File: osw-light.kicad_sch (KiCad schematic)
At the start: 53 parts, among them J1 Conn_01x02, J2 USB_C_Receptacle_USB2.0, Q1 2N7002, SW1 SW_Push, SW2 SW_Push, SW4 SW_Push, SW5 SW_Push, U1 DS3231MZ, U10 XC6209, U11 MCP73831T-2ACI_OT, U13 XC6209, U2 BMA400, U4 GC9A01_IPS_display, U6 CH340E, U7 ttgo-32-micro, U9 TPS2115A

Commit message: fixed some footprints and other stuff
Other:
- moved on the sheet: J2, R2, R3
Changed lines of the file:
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@@
   (junction (at 33.02 156.21) (diameter 0) (color 0 0 0 0)
   )
-  (junction (at 356.87 63.5) (diameter 0) (color 0 0 0 0)
+  (junction (at 340.995 72.39) (diameter 0) (color 0 0 0 0)
   )
   (junction (at 159.385 172.72) (diameter 0) (color 0 0 0 0)
@@
   (no_connect (at 217.17 86.36))
   (no_connect (at 29.21 86.36))
-  (no_connect (at 342.265 83.82))
-  (no_connect (at 342.265 86.36))
+  (no_connect (at 326.39 92.71))
+  (no_connect (at 326.39 95.25))
   (polyline (pts (xy 208.28 114.935) (xy 281.94 114.935))
     (stroke (width 0) (type default) (color 0 0 0 0))
   )
-  (wire (pts (xy 342.265 60.96) (xy 349.885 60.96))
+  (wire (pts (xy 326.39 69.85) (xy 334.01 69.85))
     (stroke (width 0) (type default) (color 0 0 0 0))
   )
@@
     (stroke (width 0) (type default) (color 0 0 0 0))
   )
-  (wire (pts (xy 354.965 60.96) (xy 356.87 60.96))
+  (wire (pts (xy 339.09 69.85) (xy 340.995 69.85))
     (stroke (width 0) (type default) (color 0 0 0 0))
   )
@@
     (stroke (width 0) (type default) (color 0 0 0 0))
   )
-  (wire (pts (xy 356.87 63.5) (xy 356.87 65.405))
+  (wire (pts (xy 340.995 72.39) (xy 340.995 74.295))
     (stroke (width 0) (type default) (color 0 0 0 0))
   )
@@
     (stroke (width 0) (type default) (color 0 0 0 0))
   )
-  (wire (pts (xy 342.265 73.66) (xy 342.265 76.2))
+  (wire (pts (xy 326.39 82.55) (xy 326.39 85.09))
     (stroke (width 0) (type default) (color 0 0 0 0))
   )
@@
     (stroke (width 0) (type default) (color 0 0 0 0))
   )
-  (wire (pts (xy 342.265 68.58) (xy 342.265 71.12))
+  (wire (pts (xy 326.39 77.47) (xy 326.39 80.01))
     (stroke (width 0) (type default) (color 0 0 0 0))
   )
@@
     (stroke (width 0) (type default) (color 0 0 0 0))
   )
-  (wire (pts (xy 356.87 63.5) (xy 349.885 63.5))
+  (wire (pts (xy 340.995 72.39) (xy 334.01 72.39))
     (stroke (width 0) (type default) (color 0 0 0 0))
   )
@@
     (stroke (width 0) (type default) (color 0 0 0 0))
   )
-  (wire (pts (xy 342.265 55.88) (xy 347.345 55.88))
+  (wire (pts (xy 326.39 64.77) (xy 331.47 64.77))
     (stroke (width 0) (type default) (color 0 0 0 0))
   )
@@
     (stroke (width 0) (type default) (color 0 0 0 0))
   )
-  (wire (pts (xy 327.025 93.98) (xy 327.025 95.885))
+  (wire (pts (xy 311.15 102.87) (xy 311.15 104.775))
     (stroke (width 0) (type default) (color 0 0 0 0))
   )
@@
     (stroke (width 0) (type default) (color 0 0 0 0))
   )
-  (wire (pts (xy 342.265 63.5) (xy 344.805 63.5))
+  (wire (pts (xy 326.39 72.39) (xy 328.93 72.39))
     (stroke (width 0) (type default) (color 0 0 0 0))
   )
@@
     (stroke (width 0) (type default) (color 0 0 0 0))
   )
-  (wire (pts (xy 356.87 60.96) (xy 356.87 63.5))
+  (wire (pts (xy 340.995 69.85) (xy 340.995 72.39))
     (stroke (width 0) (type default) (color 0 0 0 0))
   )
@@
     (effects (font (size 1.27 1.27)) (justify left bottom))
   )
-  (label "D_N" (at 342.265 71.12 0)
-    (effects (font (size 1.27 1.27)) (justify left bottom))
-  )
-  (label "VBUS" (at 347.345 55.88 180)
+  (label "D_N" (at 326.39 80.01 0)
+    (effects (font (size 1.27 1.27)) (justify left bottom))
+  )
+  (label "VBUS" (at 331.47 64.77 180)
     (effects (font (size 1.27 1.27)) (justify right bottom))
   )
@@
     (effects (font (size 1.27 1.27)) (justify left bottom))
   )
-  (label "CC2" (at 342.392 63.5 0)
+  (label "CC2" (at 326.517 72.39 0)
     (effects (font (size 1.27 1.27)) (justify left bottom))
   )
@@
     (effects (font (size 1.27 1.27)) (justify left bottom))
   )
-  (label "D_P" (at 342.265 76.2 0)
+  (label "D_P" (at 326.39 85.09 0)
     (effects (font (size 1.27 1.27)) (justify left bottom))
   )
@@
     (effects (font (size 1.27 1.27)) (justify right bottom))
   )
-  (label "CC1" (at 342.392 60.96 0)
+  (label "CC1" (at 326.517 69.85 0)
     (effects (font (size 1.27 1.27)) (justify left bottom))
   )
@@
     (pin "1")
   )
-  (symbol (lib_id "Connector:USB_C_Receptacle_USB2.0") (at 327.025 71.12 0) (unit 1)
+  (symbol (lib_id "Connector:USB_C_Receptacle_USB2.0") (at 311.15 80.01 0) (unit 1)
     (in_bom yes) (on_board yes) (fields_autoplaced)
-    (property "Reference" "J2" (id 0) (at 327.025 48.26 0))
-    (property "Value" "USB_C_Receptacle_USB2.0" (id 1) (at 327.025 50.8 0))
-    (property "Footprint" "sat1l:GCT_USB4105-GF-A" (id 2) (at 330.835 71.12 0)
-      (effects (font (size 1.27 1.27)) hide)
-    )
-    (property "Datasheet" "https://www.usb.org/sites/default/files/documents/usb_type-c.zip" (id 3) (at 330.835 71.12 0)
+    (property "Reference" "J2" (id 0) (at 311.15 57.15 0))
+    (property "Value" "USB_C_Receptacle_USB2.0" (id 1) (at 311.15 59.69 0))
+    (property "Footprint" "sat1l:GCT_USB4105-GF-A" (id 2) (at 314.96 80.01 0)
+      (effects (font (size 1.27 1.27)) hide)
+    )
+    (property "Datasheet" "https://www.usb.org/sites/default/files/documents/usb_type-c.zip" (id 3) (at 314.96 80.01 0)
       (effects (font (size 1.27 1.27)) hide)
     )
@@
     (pin "S1")
   )
-  (symbol (lib_id "Device:R_Small") (at 347.345 63.5 90) (unit 1)
+  (symbol (lib_id "Device:R_Small") (at 331.47 72.39 90) (unit 1)
     (in_bom yes) (on_board yes) (fields_autoplaced)
-    (property "Reference" "R2" (id 0) (at 347.345 57.15 90))
-    (property "Value" "5.1k" (id 1) (at 347.345 59.69 90))
-    (property "Footprint" "Resistor_SMD:R_0603_1608Metric" (id 2) (at 347.345 63.5 0)
-      (effects (font (size 1.27 1.27)) hide)
-    )
-    (property "Datasheet" "~" (id 3) (at 347.345 63.5 0)
-      (effects (font (size 1.27 1.27)) hide)
-    )
-    (pin "1")
-    (pin "2")
-  )
-  (symbol (lib_id "Device:R_Small") (at 352.425 60.96 90) (unit 1)
+    (property "Reference" "R2" (id 0) (at 331.47 66.04 90))
+    (property "Value" "5.1k" (id 1) (at 331.47 68.58 90))
+    (property "Footprint" "Resistor_SMD:R_0603_1608Metric" (id 2) (at 331.47 72.39 0)
+      (effects (font (size 1.27 1.27)) hide)
+    )
+    (property "Datasheet" "~" (id 3) (at 331.47 72.39 0)
+      (effects (font (size 1.27 1.27)) hide)
+    )
+    (pin "1")
+    (pin "2")
+  )
+  (symbol (lib_id "Device:R_Small") (at 336.55 69.85 90) (unit 1)
     (in_bom yes) (on_board yes) (fields_autoplaced)
-    (property "Reference" "R3" (id 0) (at 352.425 54.61 90))
-    (property "Value" "5.1k" (id 1) (at 352.425 57.15 90))
-    (property "Footprint" "Resistor_SMD:R_0603_1608Metric" (id 2) (at 352.425 60.96 0)
-      (effects (font (size 1.27 1.27)) hide)
-    )
-    (property "Datasheet" "~" (id 3) (at 352.425 60.96 0)
-      (effects (font (size 1.27 1.27)) hide)
-    )
-    (pin "1")
-    (pin "2")
-  )
-  (symbol (lib_id "power:GND") (at 327.025 95.885 0) (unit 1)
+    (property "Reference" "R3" (id 0) (at 336.55 63.5 90))
+    (property "Value" "5.1k" (id 1) (at 336.55 66.04 90))
+    (property "Footprint" "Resistor_SMD:R_0603_1608Metric" (id 2) (at 336.55 69.85 0)
+      (effects (font (size 1.27 1.27)) hide)
+    )
+    (property "Datasheet" "~" (id 3) (at 336.55 69.85 0)
+      (effects (font (size 1.27 1.27)) hide)
+    )
+    (pin "1")
+    (pin "2")
+  )
+  (symbol (lib_id "power:GND") (at 311.15 104.775 0) (unit 1)
     (in_bom yes) (on_board yes) (fields_autoplaced)
-    (property "Reference" "#PWR01" (id 0) (at 327.025 102.235 0)
-      (effects (font (size 1.27 1.27)) hide)
-    )
-    (property "Value" "GND" (id 1) (at 327.025 100.33 0))
-    (property "Footprint" "" (id 2) (at 327.025 95.885 0)
-      (effects (font (size 1.27 1.27)) hide)
-    )
-    (property "Datasheet" "" (id 3) (at 327.025 95.885 0)
-      (effects (font (size 1.27 1.27)) hide)
-    )
-    (pin "1")
-  )
-  (symbol (lib_id "power:GND") (at 356.87 65.405 0) (unit 1)
+    (property "Reference" "#PWR01" (id 0) (at 311.15 111.125 0)
+      (effects (font (size 1.27 1.27)) hide)
+    )
+    (property "Value" "GND" (id 1) (at 311.15 109.22 0))
+    (property "Footprint" "" (id 2) (at 311.15 104.775 0)
+      (effects (font (size 1.27 1.27)) hide)
+    )
+    (property "Datasheet" "" (id 3) (at 311.15 104.775 0)
+      (effects (font (size 1.27 1.27)) hide)
+    )
+    (pin "1")
+  )
+  (symbol (lib_id "power:GND") (at 340.995 74.295 0) (unit 1)
     (in_bom yes) (on_board yes) (fields_autoplaced)
-    (property "Reference" "#PWR02" (id 0) (at 356.87 71.755 0)
-      (effects (font (size 1.27 1.27)) hide)
-    )
-    (property "Value" "GND" (id 1) (at 356.87 69.85 0))
-    (property "Footprint" "" (id 2) (at 356.87 65.405 0)
-      (effects (font (size 1.27 1.27)) hide)
-    )
-    (property "Datasheet" "" (id 3) (at 356.87 65.405 0)
-      (effects (font (size 1.27 1.27)) hide)
-    )
+    (property "Reference" "#PWR02" (id 0) (at 340.995 80.645 0)
+      (effects (font (size 1.27 1.27)) hide)
+    )
+    (property "Value" "GND" (id 1) (at 340.995 78.74 0))
+    (property "Footprint" "" (id 2) (at 340.995 74.295 0)
+      (effects (font (size 1.27 1.27)) hide)
+    )
+    (property "Datasheet" "" (id 3) (at 340.995 74.295 0)
+      (effects (font (size 1.27 1.27)) hide)
+    )

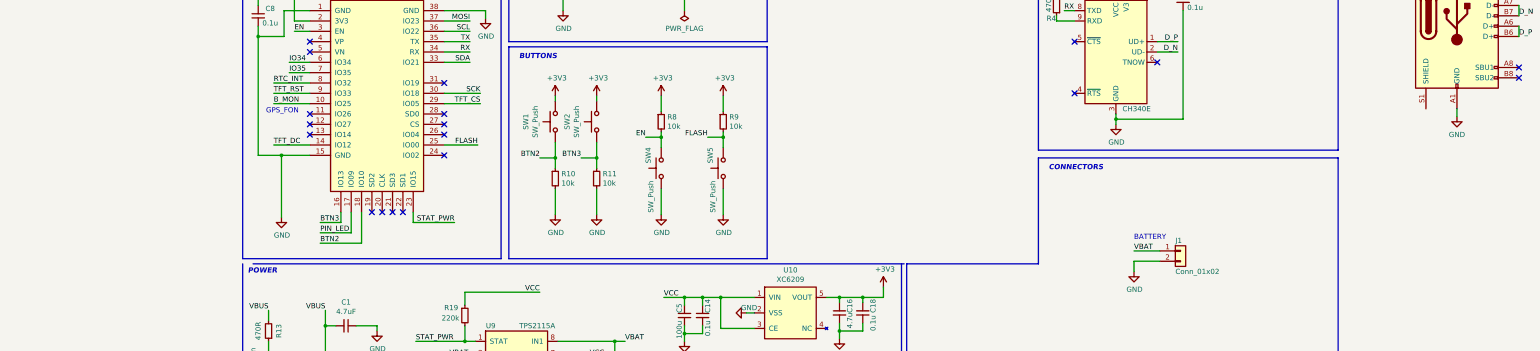
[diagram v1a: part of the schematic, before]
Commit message: Little fixes
now controller is not sticking out from the cpb, so it's (not)completely round, just before commiting i've realised that there is a display ribbon
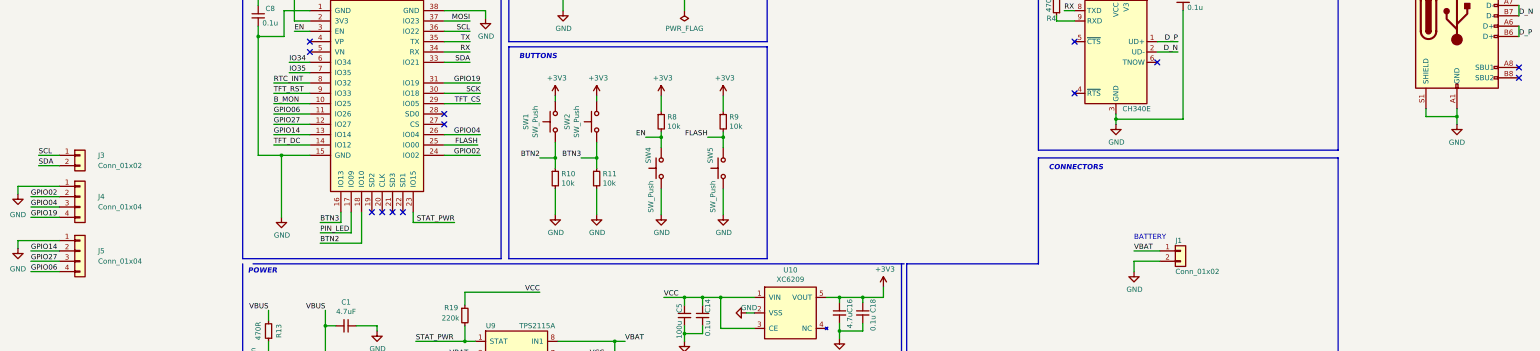
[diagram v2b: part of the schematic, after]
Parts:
- added J3: Conn_01x02, Connector_PinHeader_1.00mm:PinHeader_1x02_P1.00mm_Vertical, symbol Connector_Generic:Conn_01x02
- added J4, J5: Conn_01x04, open-Smartwatch:PinHeader_1x04_P1.00mm_Vertical, symbol open-Smartwatch:Conn_01x04
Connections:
- net GND: now also J2.S1 (SHIELD), J4.1 (Pin_1), J5.1 (Pin_1)
- net SCL: now also J3.1 (Pin_1)
- net SDA: now also J3.2 (Pin_2)
- net GPIO06: now reaches U7.11 (IO26)
- net GPIO06: now also J5.4 (Pin_4)
- net GPIO27: now reaches U7.12 (IO27)
- net GPIO27: now also J5.3 (Pin_3)
- net GPIO14: now reaches U7.13 (IO14)
- net GPIO14: now also J5.2 (Pin_2)
- net GPIO02: now reaches U7.24 (IO02)
- net GPIO02: now also J4.2 (Pin_2)
- net GPIO04: now reaches U7.26 (IO04)
- net GPIO04: now also J4.3 (Pin_3)
- net GPIO19: now reaches U7.31 (IO19)
- net GPIO19: now also J4.4 (Pin_4)
- no-connect marks 21 -> 15
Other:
- note removed: "GPS_FON"

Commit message: changed type-c to hro one, added cut on the edge for the display ribbon so everything can fit in r18.1mm circle
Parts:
- J1: footprint Connector_PinHeader_2.54mm:PinHeader_1x02_P2.54mm_Vertical -> open-Smartwatch:PinHeader_1x02_P1.0mm_Vertical
- J2: footprint sat1l:GCT_USB4105-GF-A -> Connector_USB:USB_C_Receptacle_HRO_TYPE-C-31-M-12
- J3: footprint Connector_PinHeader_1.00mm:PinHeader_1x02_P1.00mm_Vertical -> open-Smartwatch:PinHeader_1x02_P1.0mm_Vertical
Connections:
- net SCL: now also J3.2 (Pin_2); no longer J3.1 (Pin_1)
- net SDA: now also J3.1 (Pin_1); no longer J3.2 (Pin_2)
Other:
- moved on the sheet: C9, J1, J2, J3, J4, J5, R2, R3, R4, U6

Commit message: added repo link on the watch
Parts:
- J1, J3, J4, J5: now left out of the parts list
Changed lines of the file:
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@@
   )
   (symbol (lib_id "Connector_Generic:Conn_01x02") (at 194.31 149.86 0) (unit 1)
-    (in_bom yes) (on_board yes)
+    (in_bom no) (on_board yes)
     (property "Reference" "J1" (id 0) (at 193.04 147.32 0)
       (effects (font (size 1.27 1.27)) (justify left))
@@
   )
   (symbol (lib_id "open-Smartwatch:Conn_01x04") (at 231.14 147.955 0) (unit 1)
-    (in_bom yes) (on_board yes) (fields_autoplaced)
+    (in_bom no) (on_board yes) (fields_autoplaced)
     (property "Reference" "J5" (id 0) (at 235.585 147.9549 0)
       (effects (font (size 1.27 1.27)) (justify left))
@@
   )
   (symbol (lib_id "Connector_Generic:Conn_01x02") (at 231.14 124.46 0) (unit 1)
-    (in_bom yes) (on_board yes) (fields_autoplaced)
+    (in_bom no) (on_board yes) (fields_autoplaced)
     (property "Reference" "J3" (id 0) (at 235.585 124.4599 0)
       (effects (font (size 1.27 1.27)) (justify left))
@@
   )
   (symbol (lib_id "open-Smartwatch:Conn_01x04") (at 231.14 134.62 0) (unit 1)
-    (in_bom yes) (on_board yes) (fields_autoplaced)
+    (in_bom no) (on_board yes) (fields_autoplaced)
     (property "Reference" "J4" (id 0) (at 235.585 134.6199 0)
       (effects (font (size 1.27 1.27)) (justify left))

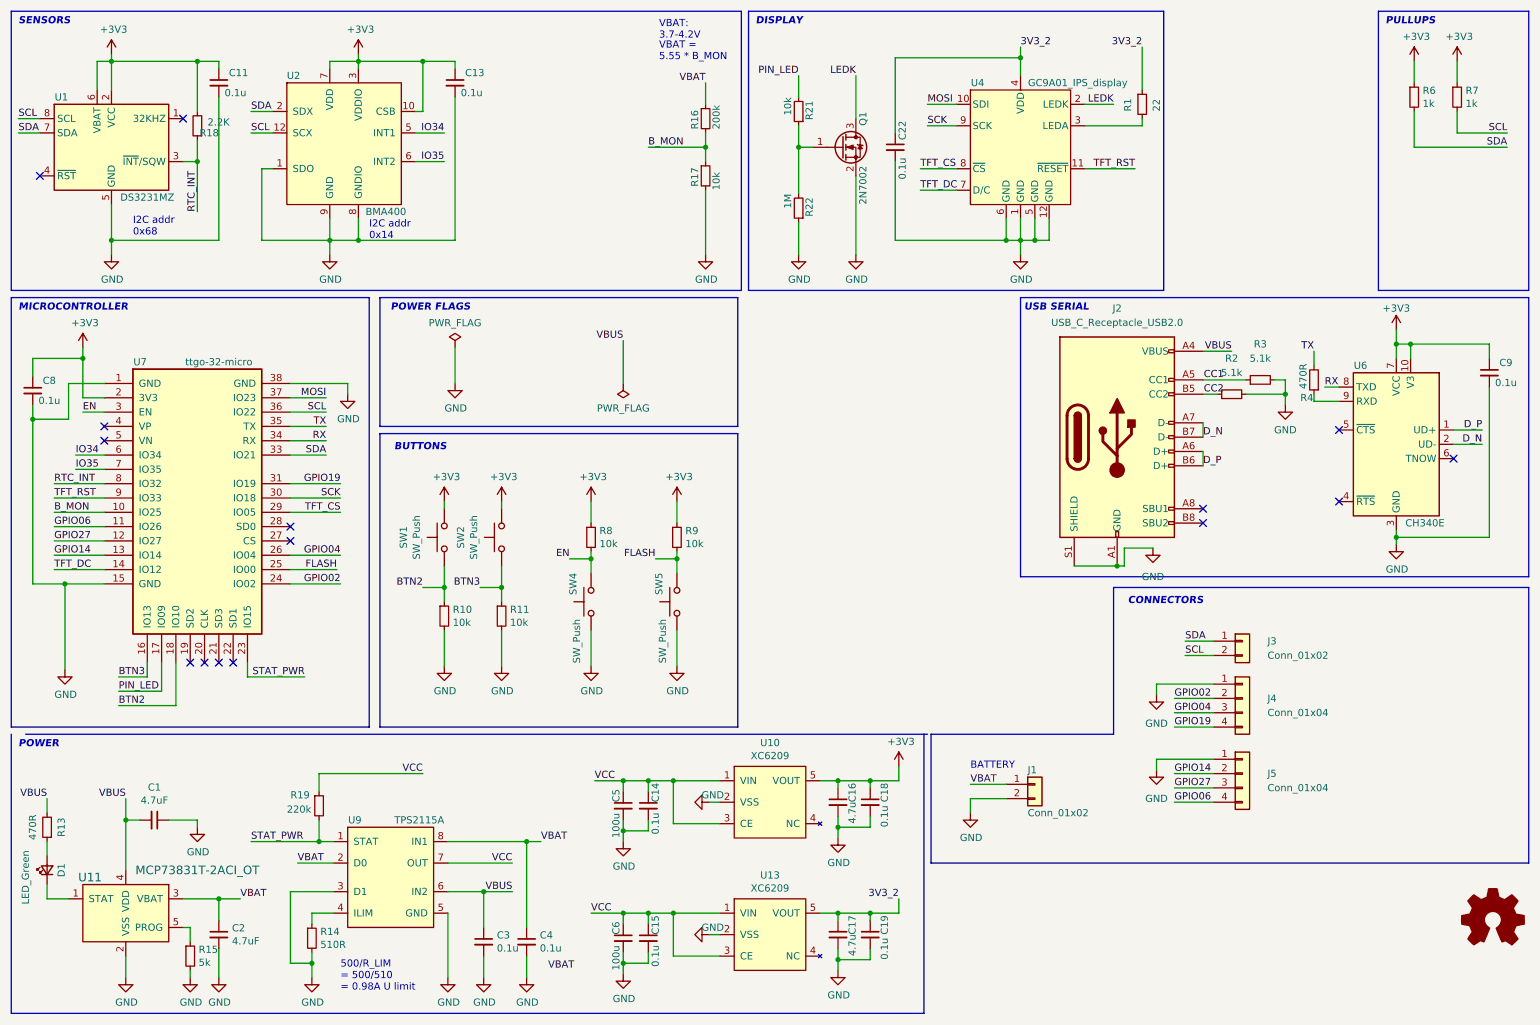
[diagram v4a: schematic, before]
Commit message: re-thought some aspects of the pcb and schematics: now there is only one ldo and pcb layout is now better for hand soldering, still needs some cleanup (and bom consolidation)
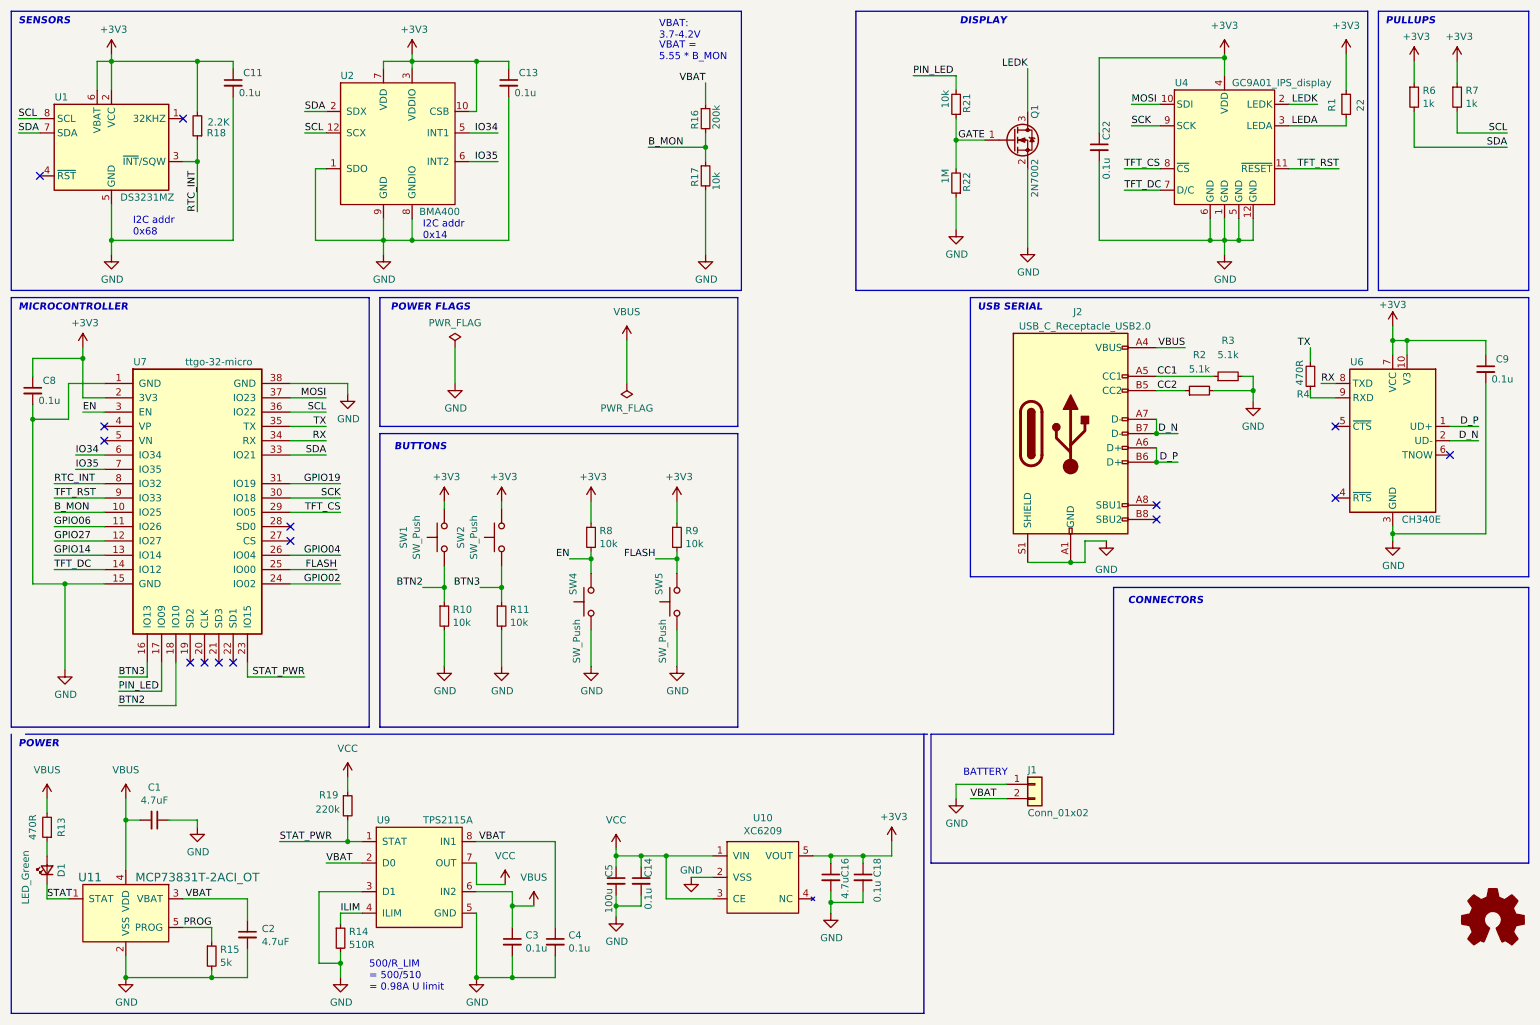
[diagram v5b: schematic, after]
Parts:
- removed C15, C19: 0.1u, Capacitor_SMD:C_0603_1608Metric, symbol Device:C_Small
- removed C17: 4.7u, Capacitor_SMD:C_0603_1608Metric, symbol Device:C_Small
- removed C6: 100u, Capacitor_SMD:C_1206_3216Metric, symbol Device:C_Small
- removed J3: Conn_01x02, open-Smartwatch:PinHeader_1x02_P1.0mm_Vertical, symbol Connector_Generic:Conn_01x02
- removed J4, J5: Conn_01x04, open-Smartwatch:PinHeader_1x04_P1.00mm_Vertical, symbol open-Smartwatch:Conn_01x04
- removed U13: XC6209, Package_TO_SOT_SMD:SOT-23-5, symbol open-Smartwatch:XC6209
- J1: footprint open-Smartwatch:PinHeader_1x02_P1.0mm_Vertical -> open-Smartwatch:batteryPads
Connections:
- net 3V3_2 is gone; now on net +3V3: C22.1, R1.1, U4.4 (VDD)
- net GND: now also J1.1 (Pin_1); no longer J1.2 (Pin_2)
- net VBAT: now also J1.2 (Pin_2); no longer J1.1 (Pin_1)
- net LEDA: now reaches R1.2, U4.3 (LEDA)
- net ILIM: now reaches R14.1, U9.4 (ILIM)
- net STAT: now reaches D1.1 (K), U11.1 (STAT)
- net PROG: now reaches R15.1, U11.5 (PROG)
- net GATE: now reaches Q1.1 (G), R21.1, R22.2
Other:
- moved on the sheet: C11, C13, C14, C16, C18, C2, C22, C3, C4, C5, C9, J2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

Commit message: wow ive did something
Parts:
- U10: value XC6209 -> XC6209F332MR-G
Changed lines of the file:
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@@
     (in_bom yes) (on_board yes)
     (property "Reference" "U10" (id 0) (at 146.05 155.829 0))
-    (property "Value" "XC6209" (id 1) (at 146.05 158.1404 0))
+    (property "Value" "XC6209F332MR-G" (id 1) (at 146.05 158.1404 0))
     (property "Footprint" "Package_TO_SOT_SMD:SOT-23-5" (id 2) (at 146.05 158.75 0)
       (effects (font (size 1.27 1.27)) hide)
@@
     )
     (path "/00000000-0000-0000-0000-000060cab8dd"
-      (reference "U10") (unit 1) (value "XC6209") (footprint "Package_TO_SOT_SMD:SOT-23-5")
+      (reference "U10") (unit 1) (value "XC6209F332MR-G") (footprint "Package_TO_SOT_SMD:SOT-23-5")
     )
     (path "/00000000-0000-0000-0000-00005f5769ac"
